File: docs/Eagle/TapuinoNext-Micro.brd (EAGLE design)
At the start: 73.6 x 44.1 mm, 10 parts

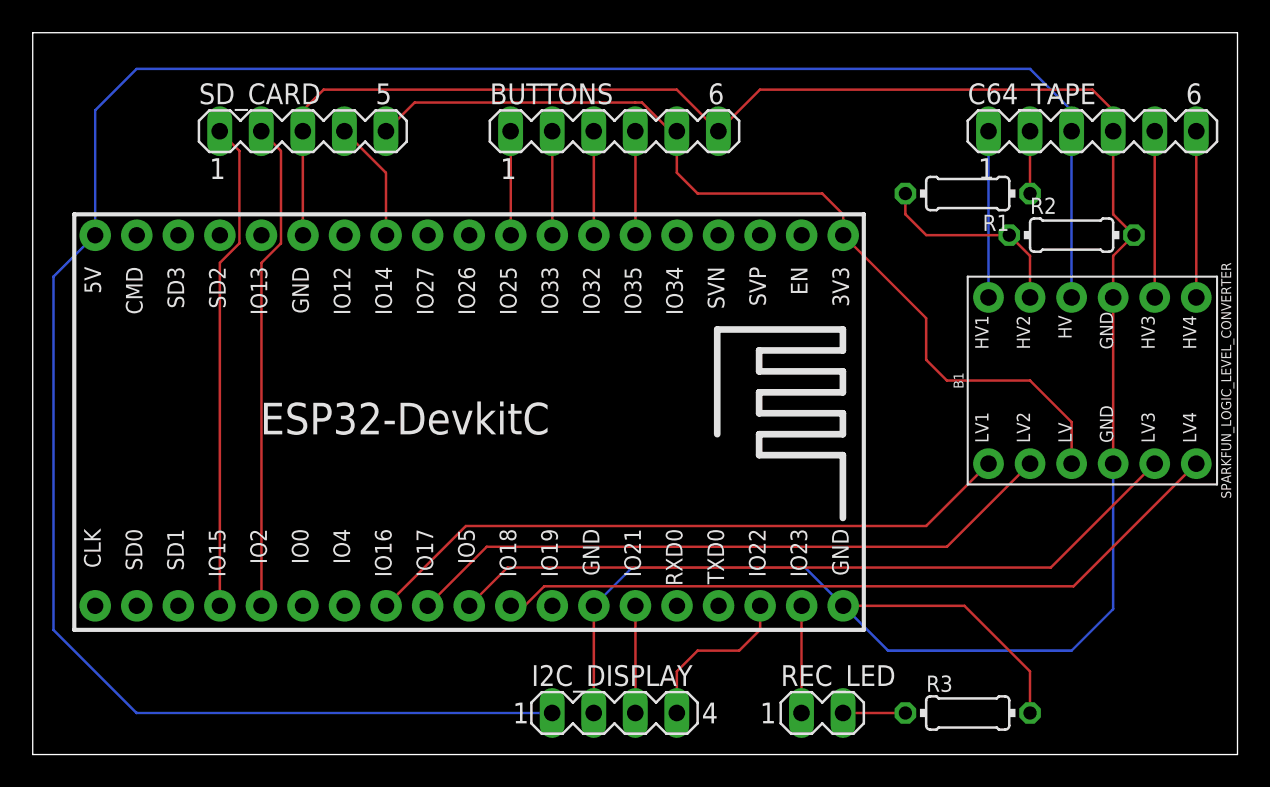
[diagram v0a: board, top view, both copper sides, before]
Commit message: fixed definition for OLED1306 added the correct part for tthe ESP32 Devkit added a micro board for system builders (trying to keep this to the smallest footprint possible for custom builds) fixed the foot print on the reference board need to sort out constant changes to config.h to allow users changes outside of source control
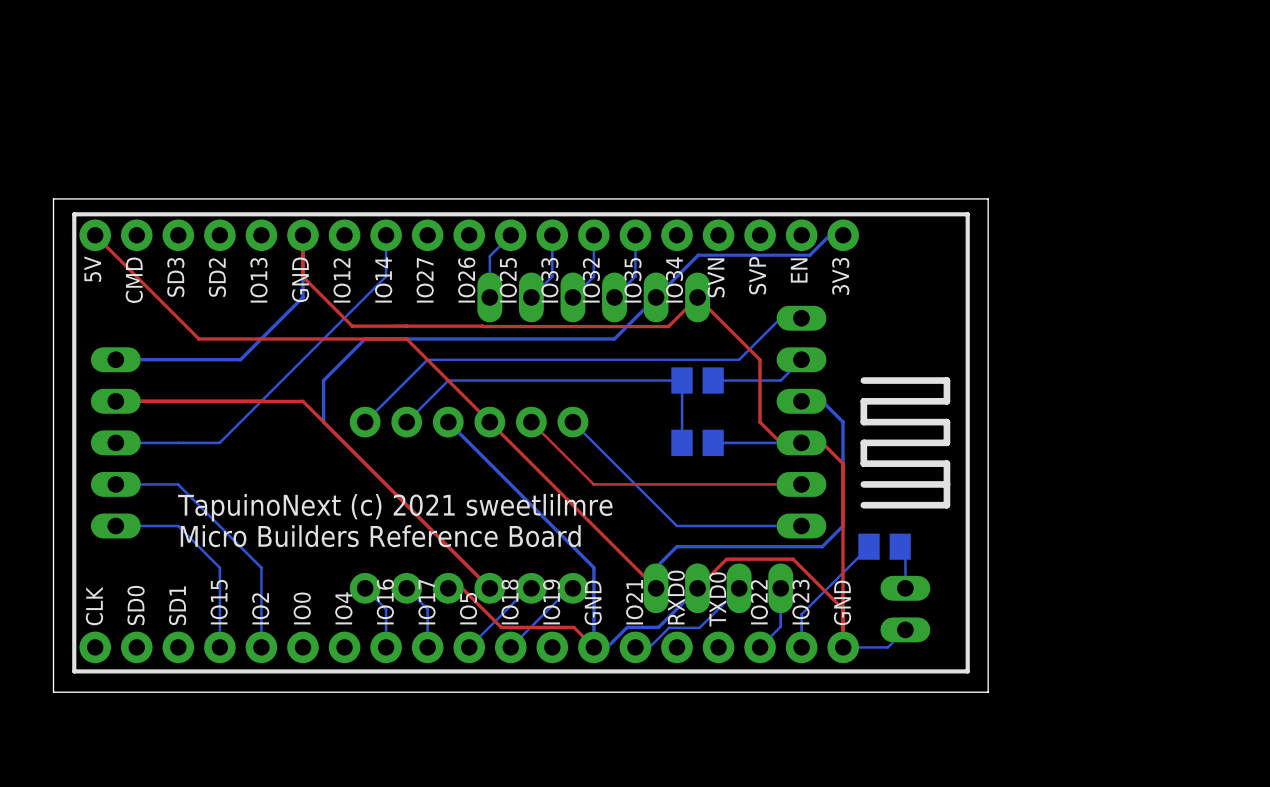
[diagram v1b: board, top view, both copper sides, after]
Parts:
- removed U$1: ESP32DEVKITC, ESP32-DEVKITC:ESP32-DEVKITC
- added U1: ESP32-DEVKITC-38, ESP32-DEVKITC-38PIN:ESP32-DEVKITC-38
- R1, R2, R3: device rcl:0204/7 -> rcl:M0805
- moved B1 38.9 mm to (45.7, 20.3), flipped to the bottom
- moved R2 26.2 mm to (59.7, 24.1), flipped to the bottom
- moved C64_TAPE 25.1 mm to (66.0, 25.4), flipped to the bottom, turned to 270 degrees
- moved SD_CARD 22.2 mm to (24.1, 24.1), flipped to the bottom, turned to 90 degrees
- moved R1 20.1 mm to (59.7, 27.9), flipped to the bottom
- moved R3 11.4 mm to (71.1, 17.8), flipped to the bottom, turned to 180 degrees
- moved BUTTONS 10.2 mm to (53.3, 33.0), flipped to the bottom, turned to 180 degrees
- moved I2C_DISPLAY 9.92 mm to (61.0, 15.2), flipped to the bottom, turned to 180 degrees
- moved REC_LED 7.41 mm to (72.4, 14.0), flipped to the bottom, turned to 270 degrees
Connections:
- removed net N$2: R3.1, REC_LED.2
- new net N$1: R3.2, REC_LED.1
- net 3V3: now also SD_CARD.4, U1.1; no longer SD_CARD.5, U$1.1
- net BTN_ABORT: now also U1.6; no longer U$1.6
- net BTN_NEXT/ROTA: now also U1.9; no longer U$1.9
- net BTN_PREV/ROTB: now also U1.7; no longer U$1.7
- net BTN_SEL/ROTARY: now also U1.8; no longer U$1.8
- net C64+5V: now also U1.19; no longer U$1.19
- net C64MOTOR: now also R1.2; no longer R1.1
- net C64MOTOR_5V: now also B1.HV3, R1.1, R2.2; no longer B1.HV2, R1.2, R2.1
- net C64READ: now also B1.HV2; no longer B1.HV3
- net C64SENSE: now also B1.HV4; no longer B1.HV1
- net C64WRITE: now also B1.HV1; no longer B1.HV4
- net GND: now also R2.1, REC_LED.2, SD_CARD.5, U1.14, U1.32, U1.38; no longer R2.2, R3.2, SD_CARD.3, U$1.14, U$1.32, U$1.38
- net MOTOR: now also B1.LV3, U1.28; no longer B1.LV2, U$1.28
- net READ: now also B1.LV2, U1.29; no longer B1.LV3, U$1.29
- net REC_LED: now also R3.1, U1.37; no longer REC_LED.1, U$1.37
- net SCL: now also U1.36; no longer U$1.36
- net SDA: now also U1.33; no longer U$1.33
- net SDCLK: now also SD_CARD.3, U1.12; no longer SD_CARD.4, U$1.12
- net SDCMD: now also U1.23; no longer U$1.23
- net SDDO: now also U1.24; no longer U$1.24
- net SENSE: now also B1.LV4, U1.27; no longer B1.LV1, U$1.27
- net WRITE: now also B1.LV1, U1.30; no longer B1.LV4, U$1.30
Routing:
- net C64+5V: track 138.6 -> 66.4 mm
- net READ: track 45.5 -> 5.30 mm
- net WRITE: track 45.5 -> 5.30 mm
- net MOTOR: track 40.4 -> 4.14 mm
- net SENSE: track 40.4 -> 4.14 mm
- net 3V3: track 57.0 -> 88.8 mm
- net C64SENSE: track 10.2 -> 29.3 mm
- net GND: track 150.3 -> 131.4 mm
- net SDCMD: track 30.0 -> 12.3 mm
- net SDCLK: track 7.42 -> 23.3 mm
- net SDDO: track 30.0 -> 15.9 mm
- net C64MOTOR_5V: track 12.5 -> 21.7 mm
- net C64READ: track 10.2 -> 18.1 mm
- net C64WRITE: track 10.2 -> 16.6 mm
- net SCL: track 10.1 -> 4.13 mm
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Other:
- board size 73.6 x 44.1 mm -> 57.1 x 30.1 mm
- board text added: "TapuinoNext (c) 2021 sweetlilmre Micro Builders Reference Board"
- board text removed: "TapuinoNext (c) 2021 sweetlilmre Minimum Reference Board"

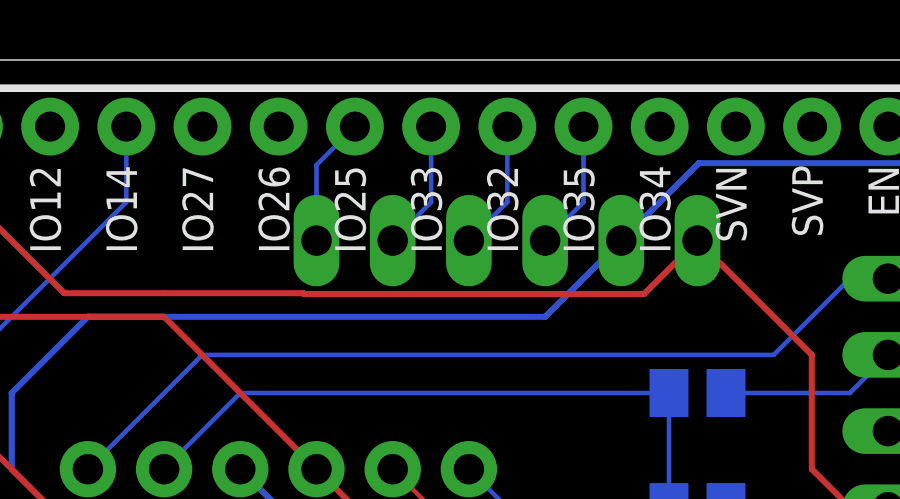
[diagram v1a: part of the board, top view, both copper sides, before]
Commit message: Changed rotary wiring back to original to match stripboard
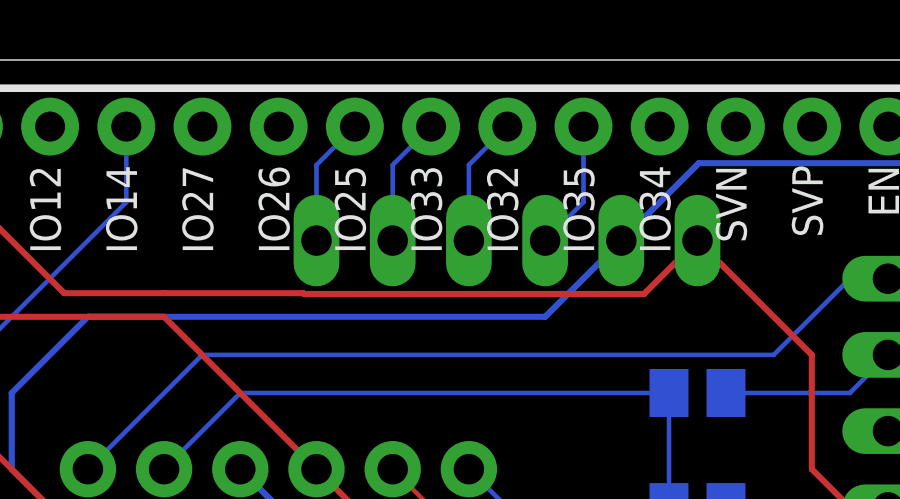
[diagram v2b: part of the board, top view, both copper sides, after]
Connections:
- net BTN_PREV/ROTB: now also BUTTONS.2, U1.8; no longer BUTTONS.3, U1.7
- net BTN_SEL/ROTARY: now also BUTTONS.3, U1.7; no longer BUTTONS.2, U1.8
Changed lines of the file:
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@@
 <layer number="14" name="Route14" color="22" fill="1" visible="no" active="no"/>
 <layer number="15" name="Route15" color="23" fill="1" visible="no" active="no"/>
-<layer number="16" name="Bottom" color="1" fill="1" visible="no" active="yes"/>
+<layer number="16" name="Bottom" color="1" fill="1" visible="yes" active="yes"/>
 <layer number="17" name="Pads" color="2" fill="1" visible="yes" active="yes"/>
 <layer number="18" name="Vias" color="2" fill="1" visible="yes" active="yes"/>
@@
 <layer number="20" name="Dimension" color="24" fill="1" visible="yes" active="yes"/>
 <layer number="21" name="tPlace" color="7" fill="1" visible="yes" active="yes"/>
-<layer number="22" name="bPlace" color="7" fill="1" visible="no" active="yes"/>
+<layer number="22" name="bPlace" color="7" fill="1" visible="yes" active="yes"/>
 <layer number="23" name="tOrigins" color="15" fill="1" visible="yes" active="yes"/>
-<layer number="24" name="bOrigins" color="15" fill="1" visible="no" active="yes"/>
+<layer number="24" name="bOrigins" color="15" fill="1" visible="yes" active="yes"/>
 <layer number="25" name="tNames" color="7" fill="1" visible="yes" active="yes"/>
-<layer number="26" name="bNames" color="7" fill="1" visible="no" active="yes"/>
+<layer number="26" name="bNames" color="7" fill="1" visible="yes" active="yes"/>
 <layer number="27" name="tValues" color="7" fill="1" visible="no" active="yes"/>
 <layer number="28" name="bValues" color="7" fill="1" visible="no" active="yes"/>
@@
 <layer number="38" name="bTest" color="7" fill="1" visible="no" active="yes"/>
 <layer number="39" name="tKeepout" color="4" fill="11" visible="yes" active="yes"/>
-<layer number="40" name="bKeepout" color="1" fill="11" visible="no" active="yes"/>
+<layer number="40" name="bKeepout" color="1" fill="11" visible="yes" active="yes"/>
 <layer number="41" name="tRestrict" color="4" fill="10" visible="yes" active="yes"/>
-<layer number="42" name="bRestrict" color="1" fill="10" visible="no" active="yes"/>
+<layer number="42" name="bRestrict" color="1" fill="10" visible="yes" active="yes"/>
 <layer number="43" name="vRestrict" color="2" fill="10" visible="no" active="yes"/>
 <layer number="44" name="Drills" color="7" fill="1" visible="no" active="yes"/>
@@
 <layer number="50" name="dxf" color="7" fill="1" visible="no" active="no"/>
 <layer number="51" name="tDocu" color="7" fill="1" visible="yes" active="yes"/>
-<layer number="52" name="bDocu" color="7" fill="1" visible="no" active="yes"/>
+<layer number="52" name="bDocu" color="7" fill="1" visible="yes" active="yes"/>
 <layer number="53" name="tGND_GNDA" color="7" fill="9" visible="no" active="no"/>
 <layer number="54" name="bGND_GNDA" color="1" fill="9" visible="no" active="no"/>
@@
 </signal>
 <signal name="BTN_PREV/ROTB">
+<contactref element="U1" pad="8"/>
+<contactref element="BUTTONS" pad="2"/>
+<wire x1="50.81" y1="36.82" x2="49.53" y2="35.54" width="0.1524" layer="16"/>
+<wire x1="49.53" y1="35.54" x2="49.53" y2="33.02" width="0.1524" layer="16"/>
+</signal>
+<signal name="BTN_SEL/ROTARY">
+<contactref element="U1" pad="7"/>
 <contactref element="BUTTONS" pad="3"/>
-<contactref element="U1" pad="7"/>
-<wire x1="53.35" y1="36.82" x2="53.35" y2="34.3" width="0.1524" layer="16"/>
-<wire x1="53.35" y1="34.3" x2="52.07" y2="33.02" width="0.1524" layer="16"/>
-</signal>
-<signal name="BTN_SEL/ROTARY">
-<contactref element="BUTTONS" pad="2"/>
-<contactref element="U1" pad="8"/>
-<wire x1="50.81" y1="36.82" x2="50.81" y2="34.3" width="0.1524" layer="16"/>
-<wire x1="50.81" y1="34.3" x2="49.53" y2="33.02" width="0.1524" layer="16"/>
+<wire x1="53.35" y1="36.82" x2="52.07" y2="35.54" width="0.1524" layer="16"/>
+<wire x1="52.07" y1="35.54" x2="52.07" y2="33.02" width="0.1524" layer="16"/>
 </signal>
 <signal name="BTN_NEXT/ROTA">

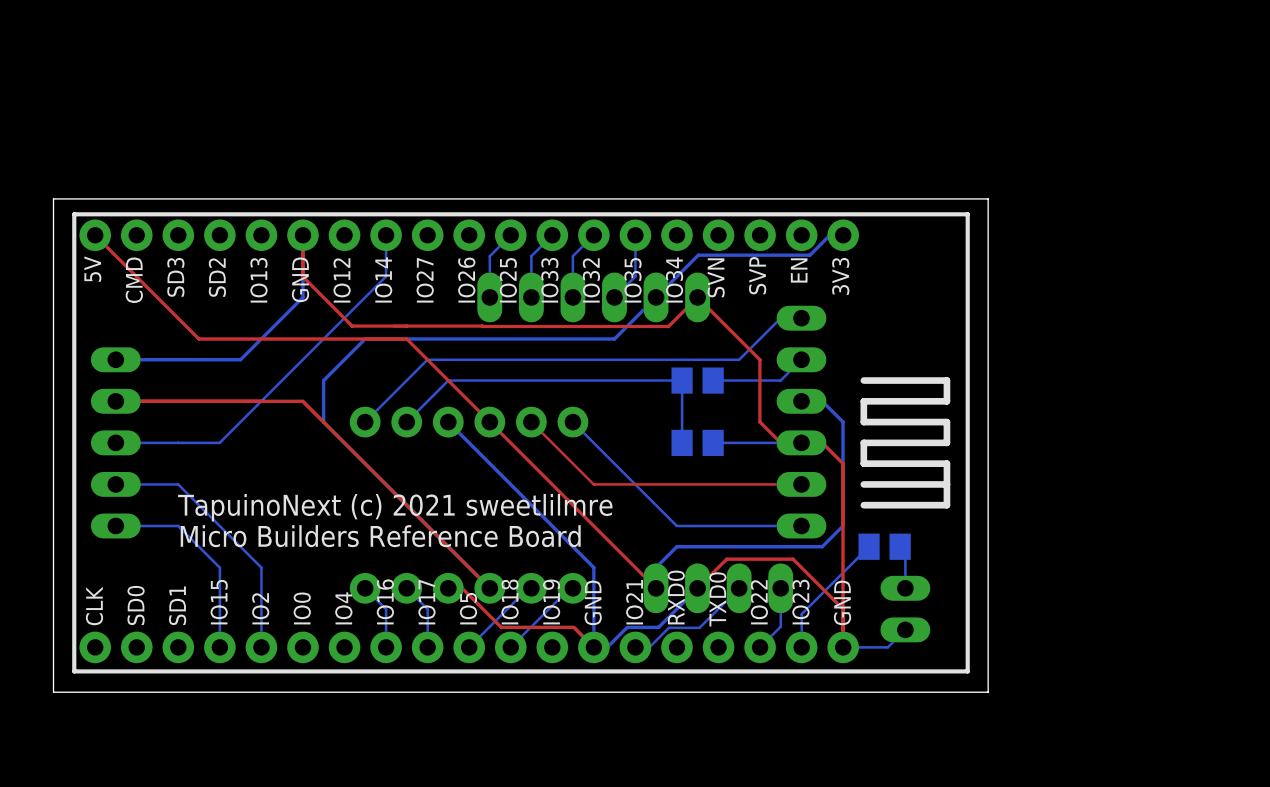
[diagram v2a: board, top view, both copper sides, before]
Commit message: Fixed pinout across all of the schematics, hopefully for the last time
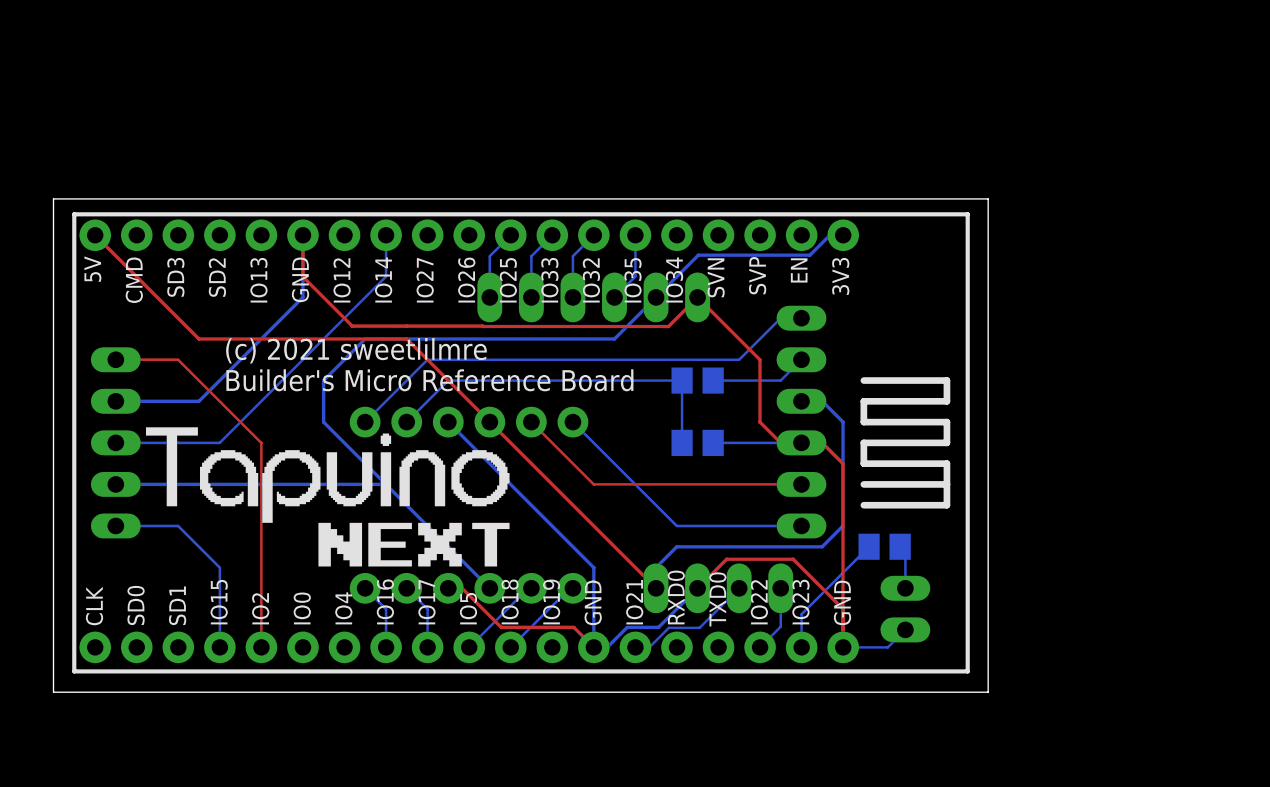
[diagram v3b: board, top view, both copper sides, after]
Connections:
- net 3V3: now also SD_CARD.2; no longer SD_CARD.4
- net GND: now also SD_CARD.4; no longer SD_CARD.5
- net SDDO: now also SD_CARD.5; no longer SD_CARD.2
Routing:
- net 3V3: track 88.8 -> 68.9 mm
- net SDDO: track 15.9 -> 23.5 mm
- net GND: track 131.4 -> 132.4 mm
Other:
- board text added: "(c) 2021 sweetlilmre Builder's Micro Reference Board"
- board text removed: "TapuinoNext (c) 2021 sweetlilmre Micro Builders Reference Board"
